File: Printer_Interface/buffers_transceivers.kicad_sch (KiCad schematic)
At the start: 13 parts, among them U1 74FCT16245, U2 74HCT245, U3 74HCT1G32, U4 74HCT1G32

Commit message: Finished schematic, review time...
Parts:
- added U22, U5: 74HCT1G32, COMET_footprints:Package_SOT23-5, symbol COMET_symbols:74x1G32
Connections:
- net +5V: now also U22.5 (VCC), U5.5 (VCC)
- net GND: now also U22.2, U22.3 (GND), U5.2, U5.3 (GND); no longer U2.5 (A4), U2.6 (A5), U2.7 (A6), U2.8 (A7), U2.9 (A8)
- new net: U2.5 (A4), U2.6 (A5), U2.7 (A6), U2.8 (A7), U2.9 (A8)
- new net SYSCLK: U22.4
- new net SYSCLK`: U22.1
- new net ~{WR`}: U5.1
- new net ~{WR}: U5.4
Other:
- moved on the sheet: U3A, U4A

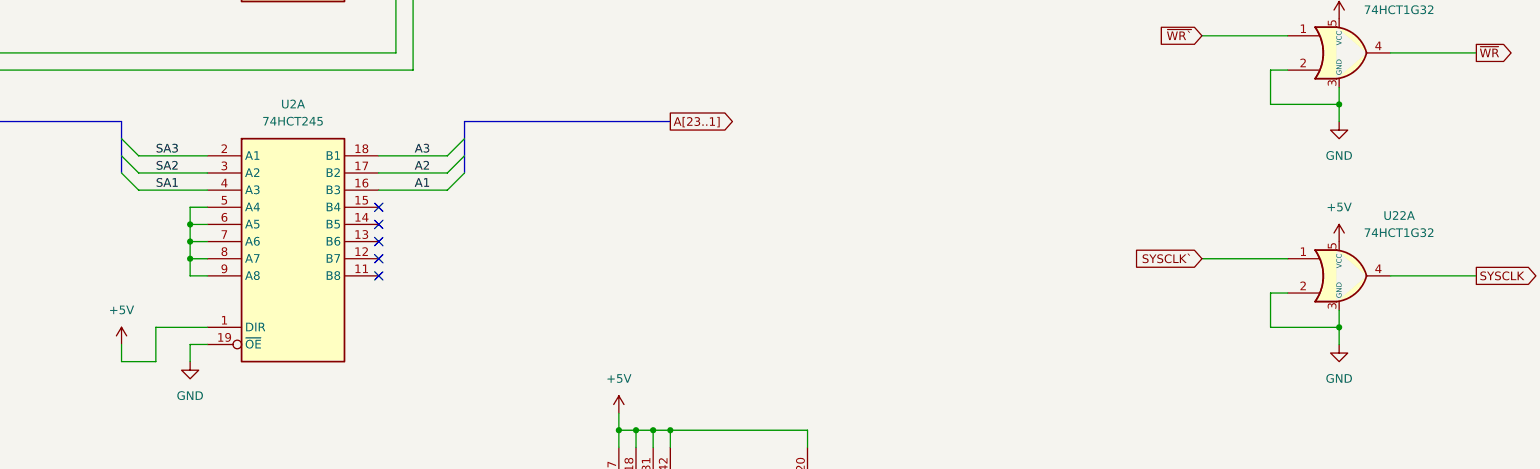
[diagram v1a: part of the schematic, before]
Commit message: Some changes
* Add pull up to DBEN to disable buffers on powerup
* A little tidying up
* Update schematic date and printout
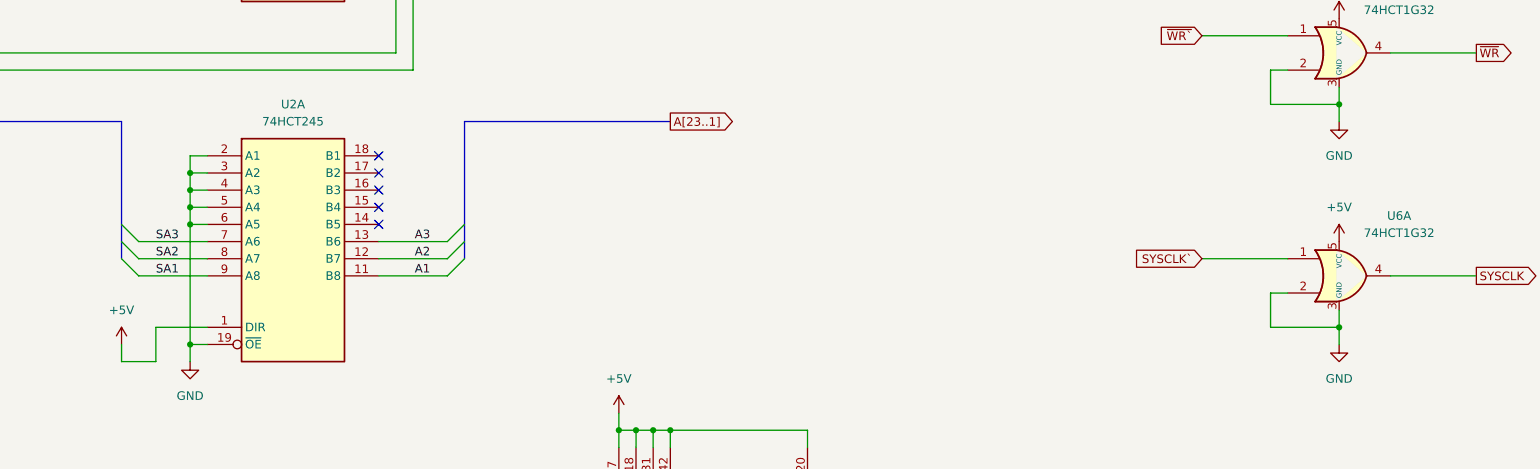
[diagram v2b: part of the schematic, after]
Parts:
- renumbered U22 to U6
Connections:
- net A1: now also U2.11 (B8); no longer U2.16 (B3)
- net A2: now also U2.12 (B7); no longer U2.17 (B2)
- net A3: now also U2.13 (B6); no longer U2.18 (B1)
- net GND: now also U2.2 (A1), U2.3 (A2), U2.4 (A3), U2.5 (A4), U2.6 (A5)
- net SA1: now also U2.9 (A8); no longer U2.4 (A3)
- net SA2: now also U2.8 (A7); no longer U2.3 (A2)
- net SA3: now also U2.7 (A6); no longer U2.2 (A1)

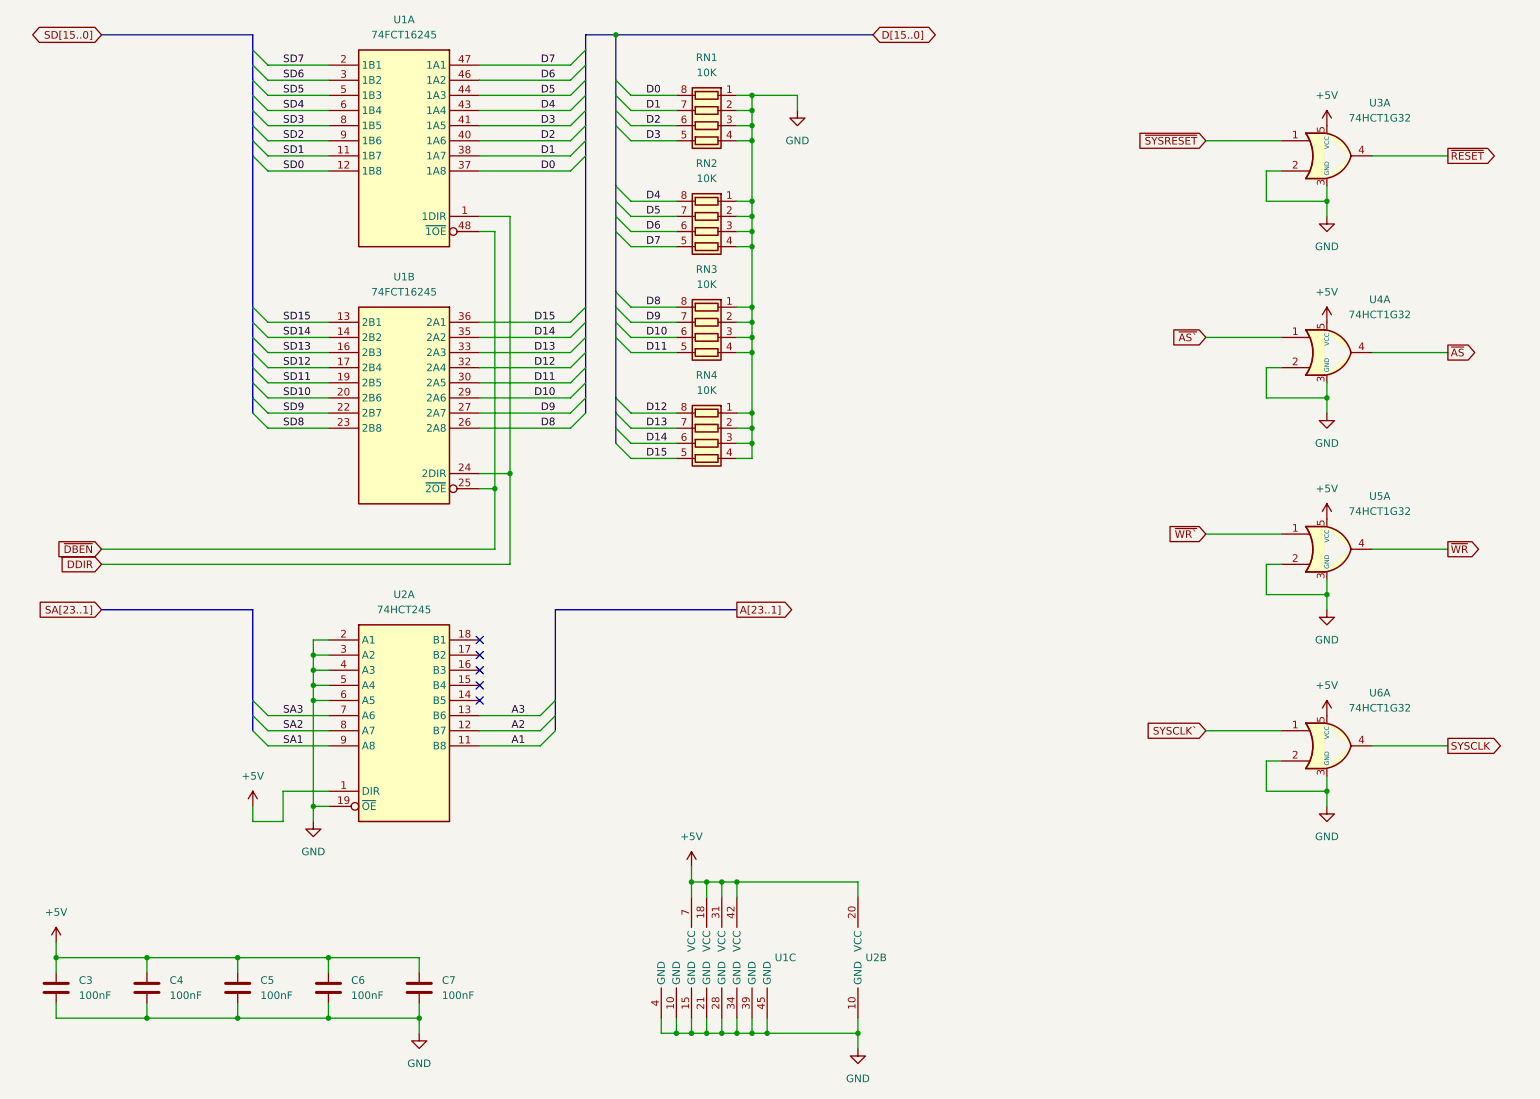
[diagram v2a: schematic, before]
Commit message: Routing complete, review time
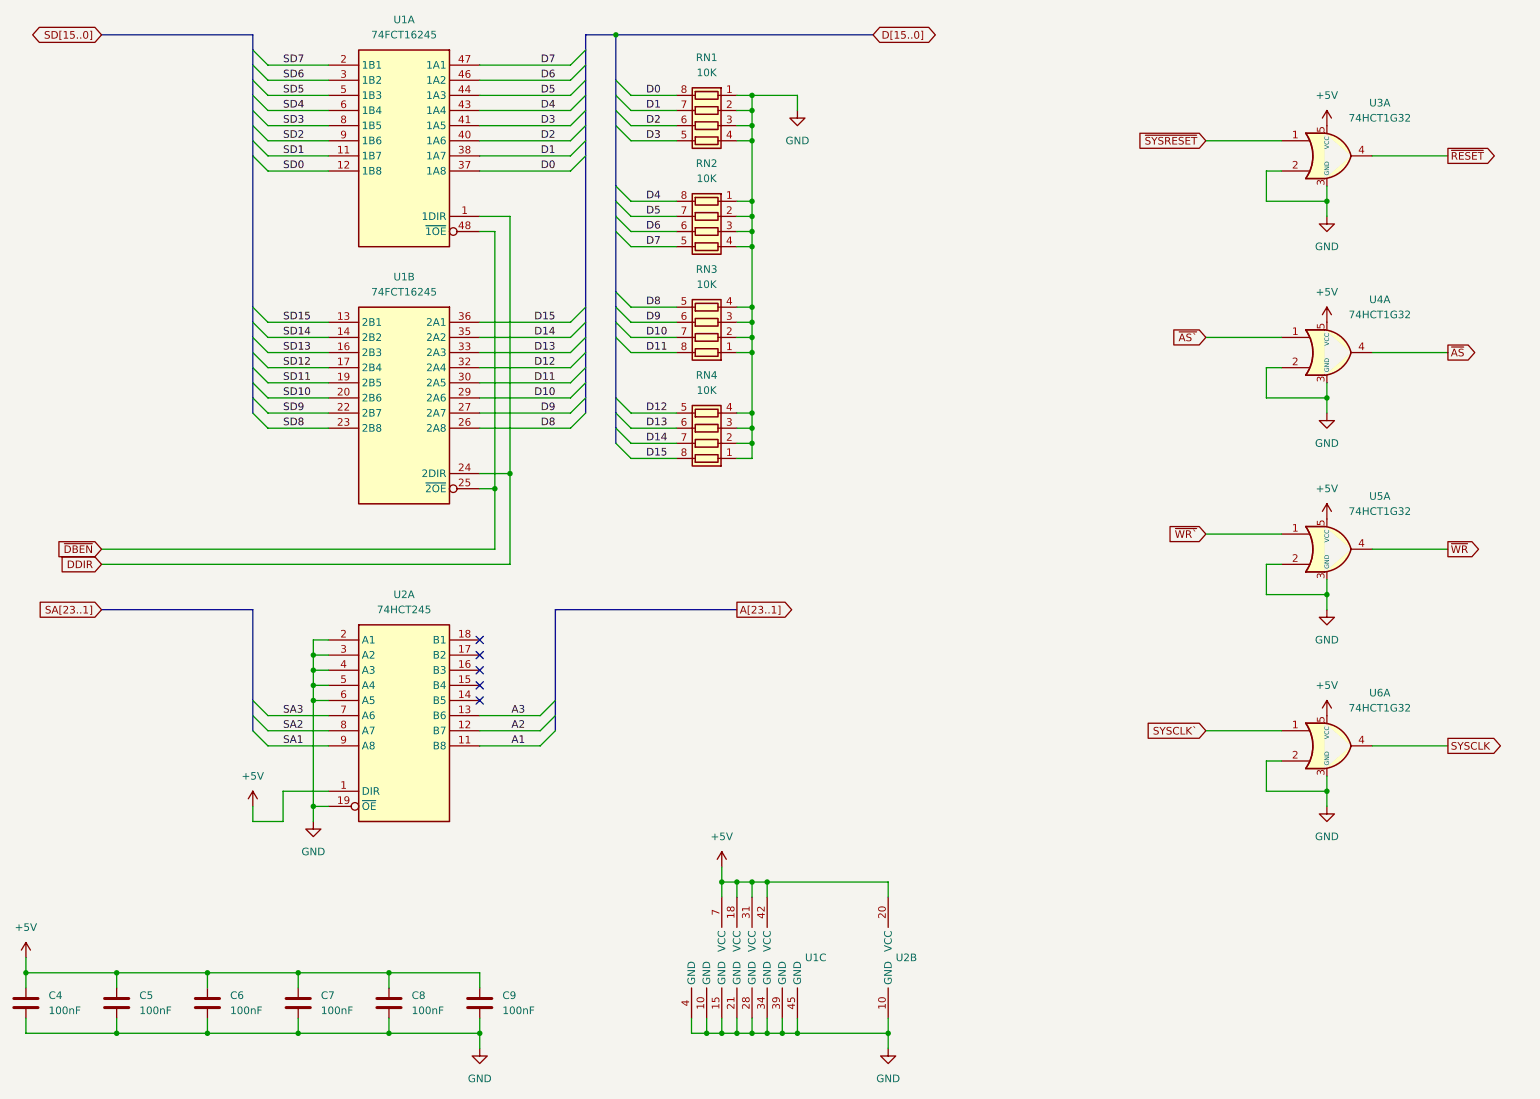
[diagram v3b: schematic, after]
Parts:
- removed C7: 100nF, COMET_footprints:C_SMD0805, symbol COMET_symbols:C
- added C8, C9: 100nF, COMET_footprints:C_SMD0805, symbol COMET_symbols:C
- renumbered C3 to C4, C4 to C5, C5 to C6, C6 to C7
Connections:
- net +5V: now also C8.1, C9.1
- net D10: now also RN3.7 (R2.2); no longer RN3.6 (R3.2)
- net D11: now also RN3.8 (R1.2); no longer RN3.5 (R4.2)
- net D12: now also RN4.5 (R4.2); no longer RN4.8 (R1.2)
- net D13: now also RN4.6 (R3.2); no longer RN4.7 (R2.2)
- net D14: now also RN4.7 (R2.2); no longer RN4.6 (R3.2)
- net D15: now also RN4.8 (R1.2); no longer RN4.5 (R4.2)
- net D8: now also RN3.5 (R4.2); no longer RN3.8 (R1.2)
- net D9: now also RN3.6 (R3.2); no longer RN3.7 (R2.2)
- net GND: now also C8.2, C9.2
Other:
- moved on the sheet: C4, C5, C6, C7, U1C, U2B

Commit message: ERC/DRC pass, clean for the most part
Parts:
- added C10: 100nF, COMET_footprints:C_SMD0805, symbol COMET_symbols:C
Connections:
- net +5V: now also C10.1
- net GND: now also C10.2
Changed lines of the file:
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@@
 	)
 	(junction
+		(at 96.52 175.26)
+		(diameter 0)
+		(color 0 0 0 0)
+	)
+	(junction
 		(at 50.8 185.42)
 		(diameter 0)
@@
 	)
 	(junction
+		(at 111.76 185.42)
+		(diameter 0)
+		(color 0 0 0 0)
+	)
+	(junction
 		(at 238.76 45.72)
 		(diameter 0)
@@
 	(wire
 		(pts
+			(xy 111.76 177.8) (xy 111.76 175.26)
+		)
+		(stroke
+			(width 0)
+			(type default)
+		)
+	)
+	(wire
+		(pts
 			(xy 20.32 175.26) (xy 35.56 175.26)
 		)
@@
 	(wire
 		(pts
-			(xy 96.52 185.42) (xy 96.52 187.96)
+			(xy 111.76 185.42) (xy 111.76 187.96)
 		)
 		(stroke
@@
 		)
 	)
+	(wire
+		(pts
+			(xy 111.76 185.42) (xy 96.52 185.42)
+		)
+		(stroke
+			(width 0)
+			(type default)
+		)
+	)
 	(bus
 		(pts
@@
 	(wire
 		(pts
+			(xy 111.76 182.88) (xy 111.76 185.42)
+		)
+		(stroke
+			(width 0)
+			(type default)
+		)
+	)
+	(wire
+		(pts
 			(xy 139.7 63.5) (xy 142.24 63.5)
 		)
@@
 	(wire
 		(pts
+			(xy 96.52 175.26) (xy 111.76 175.26)
+		)
+		(stroke
+			(width 0)
+			(type default)
+		)
+	)
+	(wire
+		(pts
 			(xy 60.96 30.48) (xy 71.12 30.48)
 		)
@@
 			)
 		)
-		(property "Description" ""
+		(property "Description" "Single 2-input OR gate"
 			(at 238.76 137.16 0)
 			(effects
@@
 			)
 		)
-		(property "Description" ""
+		(property "Description" "Dual octal bus transceiver; 3-state"
 			(at 83.82 78.74 0)
 			(effects
@@
 			)
 		)
-		(property "Description" ""
+		(property "Description" "Power symbol creates a global label with name \"+5V\""
 			(at 238.76 33.02 0)
 			(effects
@@
 			)
 		)
-		(property "Description" ""
+		(property "Description" "Power symbol creates a global label with name \"GND\" , ground"
 			(at 68.58 149.86 0)
 			(effects
@@
 			)
 		)
-		(property "Description" ""
+		(property "Description" "Power symbol creates a global label with name \"GND\" , ground"
 			(at 238.76 147.32 0)
 			(effects
@@
 			)
 		)
-		(property "Description" ""
+		(property "Description" "Power symbol creates a global label with name \"+5V\""
 			(at 238.76 99.06 0)
 			(effects
@@
 			)
 		)
-		(property "Description" ""
+		(property "Description" "Single 2-input OR gate"
 			(at 238.76 71.12 0)
 			(effects
@@
 			)
 		)
-		(property "Description" ""
+		(property "Description" "4 resistor network, parallel topology"
 			(at 134.62 33.02 0)
 			(effects
@@
 	)
 	(symbol
+		(lib_id "COMET_symbols:C")
+		(at 111.76 180.34 0)
+		(unit 1)
+		(exclude_from_sim no)
+		(in_bom yes)
+		(on_board yes)
+		(dnp no)
+		(fields_autoplaced yes)
+		(property "Reference" "C10"
+			(at 115.57 179.0699 0)
+			(effects
+				(font
+					(size 1.27 1.27)
+				)
+				(justify left)
+			)
+		)
+		(property "Value" "100nF"
+			(at 115.57 181.6099 0)
+			(effects
+				(font
+					(size 1.27 1.27)
+				)
+				(justify left)
+			)
+		)
+		(property "Footprint" "COMET_footprints:C_SMD0805"
+			(at 111.76 180.34 0)
+			(effects
+				(font
+					(size 1.27 1.27)
+				)
+				(hide yes)
+			)
+		)
+		(property "Datasheet" ""
+			(at 111.76 180.34 0)
+			(effects
+				(font
+					(size 1.27 1.27)
+				)
+				(hide yes)
+			)
+		)
+		(property "Description" ""
+			(at 111.76 180.34 0)
+			(effects
+				(font
+					(size 1.27 1.27)
+				)
+				(hide yes)
+			)
+		)
+		(pin "1"
+		)
+		(pin "2"
+		)
+		(instances
+			(project "Printer_Interface"
+				(path "/75b66dbb-7202-4875-8695-2c14dee692f0/f4191360-82a0-499d-bb29-833bf852803f"
+					(reference "C10")
+					(unit 1)
+				)
+			)
+		)
+	)
+	(symbol
 		(lib_id "power:GND")
 		(at 238.76 48.26 0)
@@
 			)
 		)
-		(property "Description" ""
+		(property "Description" "Power symbol creates a global label with name \"GND\" , ground"
 			(at 238.76 48.26 0)
 			(effects
@@
 			)
 		)
-		(property "Description" ""
+		(property "Description" "Power symbol creates a global label with name \"GND\" , ground"
 			(at 165.1 187.96 0)
 			(effects
@@
 			)
 		)
-		(property "Description" ""
+		(property "Description" "4 resistor network, parallel topology"
 			(at 134.62 50.8 0)
 			(effects
@@
 			)
 		)
-		(property "Description" ""
+		(property "Description" "4 resistor network, parallel topology"
 			(at 134.62 66.04 0)
 			(effects
@@
 	(symbol
 		(lib_id "power:GND")
-		(at 96.52 187.96 0)
+		(at 111.76 187.96 0)
 		(unit 1)
 		(exclude_from_sim no)
@@
 		(fields_autoplaced yes)
 		(property "Reference" "#PWR09"
-			(at 96.52 194.31 0)
+			(at 111.76 194.31 0)
 			(effects
 				(font
@@
 		)
 		(property "Value" "GND"
-			(at 96.52 193.04 0)
+			(at 111.76 193.04 0)
 			(effects
 				(font
@@
 		)
 		(property "Footprint" ""
-			(at 96.52 187.96 0)
+			(at 111.76 187.96 0)
 			(effects
 				(font
@@
 		)
 		(property "Datasheet" ""
-			(at 96.52 187.96 0)
+			(at 111.76 187.96 0)
 			(effects
 				(font
@@
 			)
 		)
-		(property "Description" ""
-			(at 96.52 187.96 0)
+		(property "Description" "Power symbol creates a global label with name \"GND\" , ground"
+			(at 111.76 187.96 0)
 			(effects
 				(font
@@
 			)
 		)
-		(property "Description" ""
+		(property "Description" "Power symbol creates a global label with name \"+5V\""
 			(at 20.32 172.72 0)
 			(effects
@@
 			)
 		)
-		(property "Description" ""
+		(property "Description" "Single 2-input OR gate"
 			(at 238.76 38.1 0)
 			(effects
@@
 			)
 		)
-		(property "Description" ""
+		(property "Description" "Power symbol creates a global label with name \"+5V\""
 			(at 137.16 157.48 0)
 			(effects
@@
 			)
 		)
-		(property "Description" ""
+		(property "Description" "Power symbol creates a global label with name \"+5V\""
 			(at 238.76 132.08 0)
 			(effects
@@
 			)
 		)
-		(property "Description" ""
+		(property "Description" "Single 2-input OR gate"
 			(at 238.76 38.1 0)
 			(effects
@@
 			)
 		)
-		(property "Description" ""
+		(property "Description" "4 resistor network, parallel topology"
 			(at 134.62 83.82 0)
 			(effects
@@
 			)
 		)
-		(property "Description" ""
+		(property "Description" "Single 2-input OR gate"
 			(at 238.76 137.16 0)
 			(effects
@@
 			)
 		)
-		(property "Description" ""
+		(property "Description" "Single 2-input OR gate"
 			(at 238.76 71.12 0)
 			(effects
@@
 			)
 		)
-		(property "Description" ""
+		(property "Description" "Power symbol creates a global label with name \"GND\" , ground"
 			(at 238.76 114.3 0)
 			(effects
@@
 			)
 		)
-		(property "Description" ""
+		(property "Description" "Octal bus transceiver; 3-state"
 			(at 165.1 172.72 0)
 			(effects
@@
 			)
 		)
-		(property "Description" ""
+		(property "Description" "Dual octal bus transceiver; 3-state"
 			(at 83.82 35.56 0)
 			(effects
@@
 			)
 		)
-		(property "Description" ""
+		(property "Description" "Single 2-input OR gate"
 			(at 238.76 104.14 0)
 			(effects
@@
 			)
 		)
-		(property "Description" ""
+		(property "Description" "Power symbol creates a global label with name \"GND\" , ground"
 			(at 238.76 81.28 0)
 			(effects
@@
 			)
 		)
-		(property "Description" ""
+		(property "Description" "Power symbol creates a global label with name \"+5V\""
 			(at 58.42 147.32 0)
 			(effects
@@
 			)
 		)
-		(property "Description" ""
+		(property "Description" "Power symbol creates a global label with name \"+5V\""
 			(at 238.76 66.04 0)
 			(effects
@@
 			)
 		)
-		(property "Description" ""
+		(property "Description" "Power symbol creates a global label with name \"GND\" , ground"
 			(at 149.86 30.48 0)
 			(effects
@@
 			)
 		)
-		(property "Description" ""
+		(property "Description" "Dual octal bus transceiver; 3-state"
 			(at 139.7 172.72 0)
 			(effects
@@
 			)
 		)
-		(property "Description" ""
+		(property "Description" "Single 2-input OR gate"
 			(at 238.76 104.14 0)
 			(effects
@@
 			)
 		)
-		(property "Description" ""
+		(property "Description" "Octal bus transceiver; 3-state"
 			(at 83.82 132.08 0)
 			(effects
